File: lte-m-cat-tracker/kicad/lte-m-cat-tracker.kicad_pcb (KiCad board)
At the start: 2 copper layers, 30 x 35 mm, 32 parts, among them J1 JST-GH-1.25mm-2P, J2 USB-C-16P, SW1 MSK12C02, U1 SIM7080G-M, U2 ESP32-C3, U3 LIS2DW12TR, U4 TP4056, U5 XC6220B331MR-G

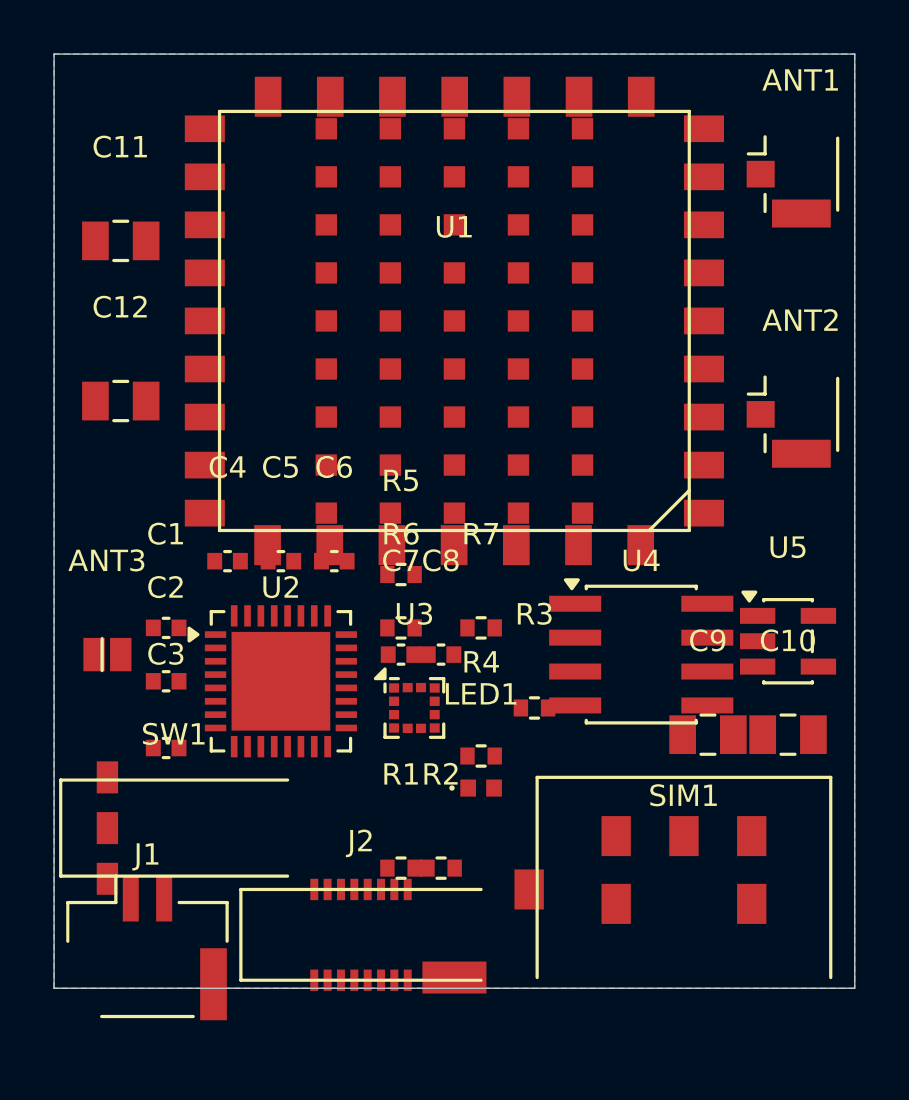
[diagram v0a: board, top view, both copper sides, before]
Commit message: lte-m-cat-tracker: PCB配置最適化・DRC短絡解消中
- PLACEMENTS全面再設計: SIM1右下端配置・SW1左側中段配置
- shorting_items: 6→1件に削減
- courtyards_overlap: 15→7件に削減
- 判明した実寸情報:
  - C9/C10 (C_0402): pad offset±0.95mm, courtyard 3.4×1.96mm
  - U4 SOIC-8: CrtYd 7.40×5.40mm (fp_lineで定義)
  - U5 SOT-23-5: CrtYd 4.10×3.40mm (fp_lineで定義)
  - generate_pcb.pyはfp_lineを未コピー → U4/U5のCrtYdがPCBに未反映

残課題:
- C9/C10短絡(1件): 0.95mm padのため3.1mm以上の間隔が必要
- U4 CrtYd 7.40×5.40mm → C9/C10の配置に影響
- generate_pcb.py の fp_line コピー対応が必要

Co-Authored-By: Claude Sonnet 4.6 <noreply@anthropic.com>
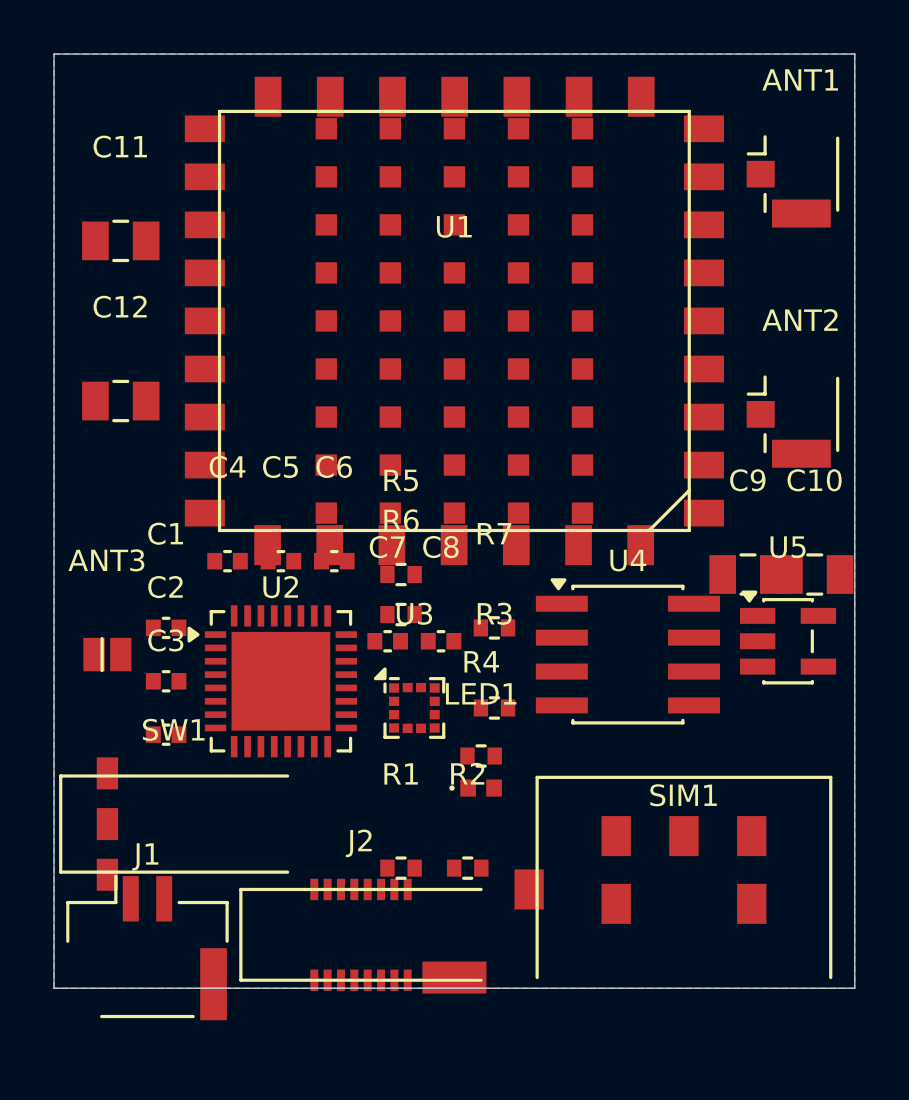
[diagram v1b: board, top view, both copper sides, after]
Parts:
- moved C9 6.18 mm to (26.0, 19.5)
- moved C10 6.08 mm to (28.5, 19.5)
- moved R3 1.50 mm to (16.5, 24.5)
- moved R2 1.00 mm to (15.5, 30.5)
- moved C7 0.71 mm to (12.5, 22.0)
- moved C3 0.50 mm to (4.20, 25.5)
- moved C8 0.50 mm to (14.5, 22.0)
- moved R6 0.50 mm to (13.0, 21.0)
- moved R7 0.50 mm to (16.5, 21.5)
- moved U4 0.50 mm to (21.5, 22.5)
- moved SW1 0.15 mm to (4.50, 28.9)
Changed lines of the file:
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@@
 	(footprint ""
 		(layer "F.Cu")
-		(at 4.2000 26.0000)
+		(at 4.2000 25.5000)
 		(property "Reference" "C3"
 			(at 0 -3.5 0)
@@
 	(footprint ""
 		(layer "F.Cu")
-		(at 13.0000 21.5000)
+		(at 13.0000 21.0000)
 		(property "Reference" "R6"
 			(at 0 -3.5 0)
@@
 	(footprint ""
 		(layer "F.Cu")
-		(at 16.0000 21.5000)
+		(at 16.5000 21.5000)
 		(property "Reference" "R7"
 			(at 0 -3.5 0)
@@
 	(footprint ""
 		(layer "F.Cu")
-		(at 13.0000 22.5000)
+		(at 12.5000 22.0000)
 		(property "Reference" "C7"
 			(at 0 -3.5 0)
@@
 	(footprint ""
 		(layer "F.Cu")
-		(at 14.5000 22.5000)
+		(at 14.5000 22.0000)
 		(property "Reference" "C8"
 			(at 0 -3.5 0)
@@
 	(footprint ""
 		(layer "F.Cu")
-		(at 22.0000 22.5000)
+		(at 21.5000 22.5000)
 		(property "Reference" "U4"
 			(at 0 -3.5 0)
@@
 	(footprint ""
 		(layer "F.Cu")
-		(at 24.5000 25.5000)
+		(at 26.0000 19.5000)
 		(property "Reference" "C9"
 			(at 0 -3.5 0)
@@
 	(footprint ""
 		(layer "F.Cu")
-		(at 27.5000 25.5000)
+		(at 28.5000 19.5000)
 		(property "Reference" "C10"
 			(at 0 -3.5 0)
@@
 	(footprint ""
 		(layer "F.Cu")
-		(at 18.0000 24.5000)
+		(at 16.5000 24.5000)
 		(property "Reference" "R3"
 			(at 0 -3.5 0)
@@
 	(footprint ""
 		(layer "F.Cu")
-		(at 4.5000 29.0000)
+		(at 4.5000 28.8500)
 		(property "Reference" "SW1"
 			(at 0 -3.5 0)
@@
 	(footprint ""
 		(layer "F.Cu")
-		(at 14.5000 30.5000)
+		(at 15.5000 30.5000)
 		(property "Reference" "R2"
 			(at 0 -3.5 0)

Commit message: lte-m-cat-tracker: DRC短絡0件・courtyard重なり0件に解消
- 短絡(C9pad2 GND ↔ C10pad1 +3.3V): C9を移動して解消
- courtyard重なり7件: C9/C10/C7/J1/J2を再配置して全解消
- DRC 149件 → 142件（shorting_items/courtyards_overlap = 0）
- 残り142件はシルク・クリアランス・エッジ系（配線前段階として正常）
- 次: 配線（ルーティング）フェーズ

Co-Authored-By: Claude Sonnet 4.6 <noreply@anthropic.com>
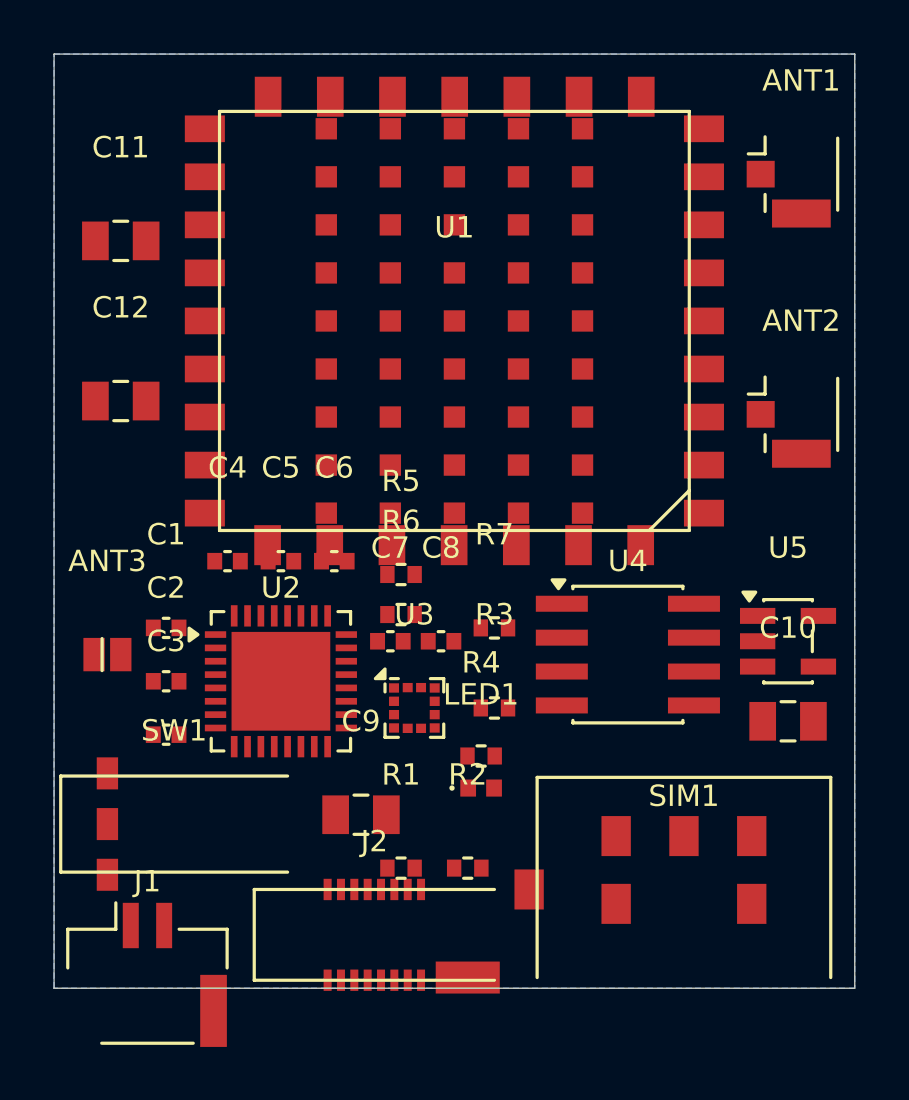
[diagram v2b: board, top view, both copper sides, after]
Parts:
- moved C9 17.1 mm to (11.5, 28.5)
- moved C10 5.59 mm to (27.5, 25.0)
- moved J1 1.00 mm to (3.50, 34.5)
- moved J2 0.50 mm to (12.0, 33.0)
- moved C7 0.10 mm to (12.6, 22.0)
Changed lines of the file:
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@@
 	(footprint ""
 		(layer "F.Cu")
-		(at 12.5000 22.0000)
+		(at 12.6000 22.0000)
 		(property "Reference" "C7"
 			(at 0 -3.5 0)
@@
 	(footprint ""
 		(layer "F.Cu")
-		(at 26.0000 19.5000)
+		(at 11.5000 28.5000)
 		(property "Reference" "C9"
 			(at 0 -3.5 0)
@@
 	(footprint ""
 		(layer "F.Cu")
-		(at 28.5000 19.5000)
+		(at 27.5000 25.0000)
 		(property "Reference" "C10"
 			(at 0 -3.5 0)
@@
 	(footprint ""
 		(layer "F.Cu")
-		(at 3.5000 33.5000)
+		(at 3.5000 34.5000)
 		(property "Reference" "J1"
 			(at 0 -3.5 0)
@@
 	(footprint ""
 		(layer "F.Cu")
-		(at 11.5000 33.0000)
+		(at 12.0000 33.0000)
 		(property "Reference" "J2"
 			(at 0 -3.5 0)

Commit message: lte-m-cat-tracker: 配置最終調整・GNDゾーン追加
- C5/C6をy=19.0→19.8、R5をy=19.5→19.8に移動
  (U1 SIM7080G-M底面パッドとの0mm重複を全解消)
- R1をy=30.5→30.2、R2をy=30.5→29.8に移動
  (J2 USB-Cとのクリアランス 0.08mm→0.38mm以上に改善)
- F.Cu GNDカッパーフィルゾーン追加 (B.Cuは既存)
  → GND未配線86→59本に削減(27本自動解決)
- 致命的違反(shorts/courtyard/0mm): 0件を維持
- DRC: 142件→131件、未配線: 86→59本
- 次フェーズ: KiCad GUIで配線(VBAT/3V3/RF/UART/I2C/SIM)

Co-Authored-By: Claude Sonnet 4.6 <noreply@anthropic.com>
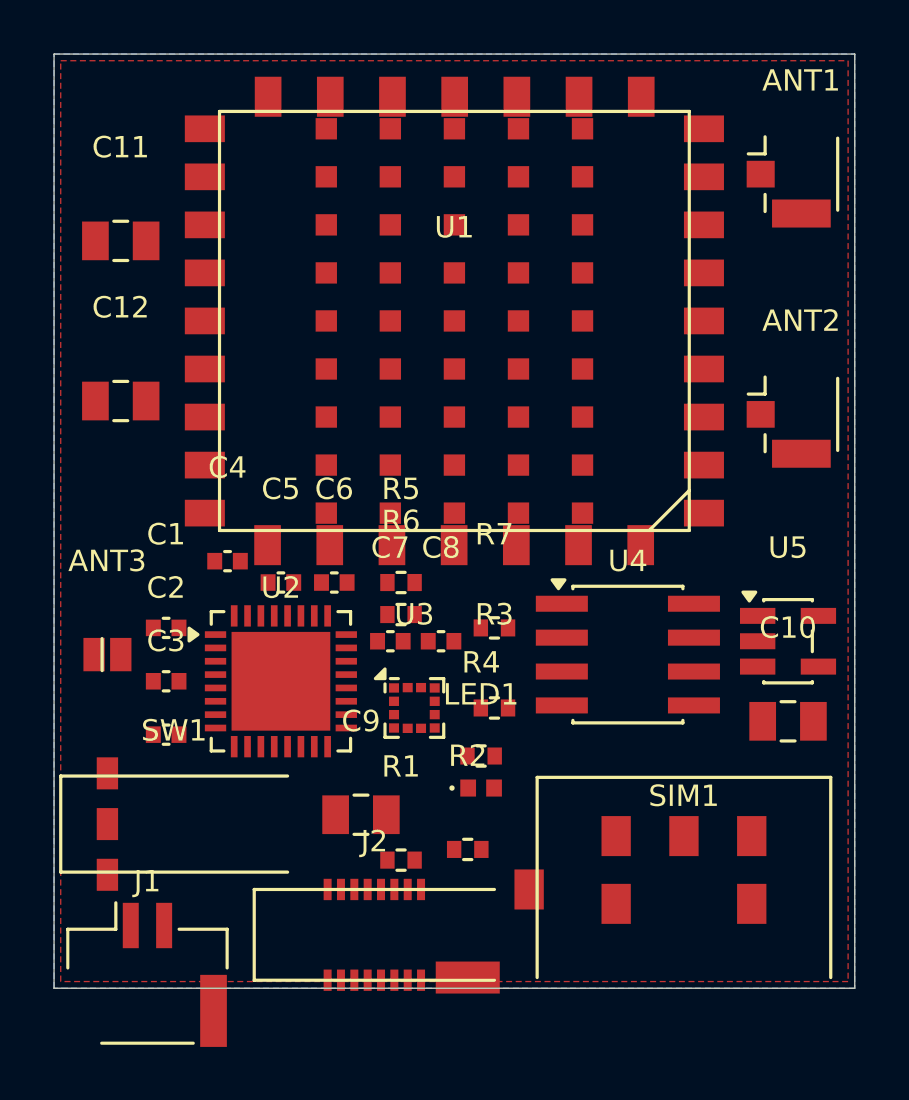
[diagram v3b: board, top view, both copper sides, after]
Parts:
- moved C5 0.80 mm to (8.50, 19.8)
- moved C6 0.80 mm to (10.5, 19.8)
- moved R2 0.70 mm to (15.5, 29.8)
- moved R1 0.30 mm to (13.0, 30.2)
- moved R5 0.30 mm to (13.0, 19.8)
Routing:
- added copper zone on F.Cu, net GND

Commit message: route_pcb_v5.py: 短絡8→0件達成（2026-06-06）
修正内容:
- SIM_TXD: B.Cu水平y=20.5→20.5（維持）、via x=9.25→11.0、B.Cu終端y=20.5
- SIM_TXD: SIM_TXD縦 x=11.0→11.5に移動（SIM_RXD via用スペース確保）
- +3.3V U2接続: via(7.5,19.6)→via(6.5,19.6)、x=7.0→6.5へ移動（C4.pad2回避）
- +3.3V U3接続: B.Cu縦スタブ x=11.5→11.8（U2右側パッドとの距離確保）
- SIM_STATUS: x=5.8→維持
- SIM_RXD: B.Cu縦x=8.75をy=20.0で止める（thermal pad干渉回避・GUI手動接続必要）

残り作業:
- SIM_RXD U2.pad28接続（KiCad GUI手動）
- VUSB接続（GUI手動）
- RF配線3本（GUI手動）

Co-Authored-By: Claude Sonnet 4.6 <noreply@anthropic.com>
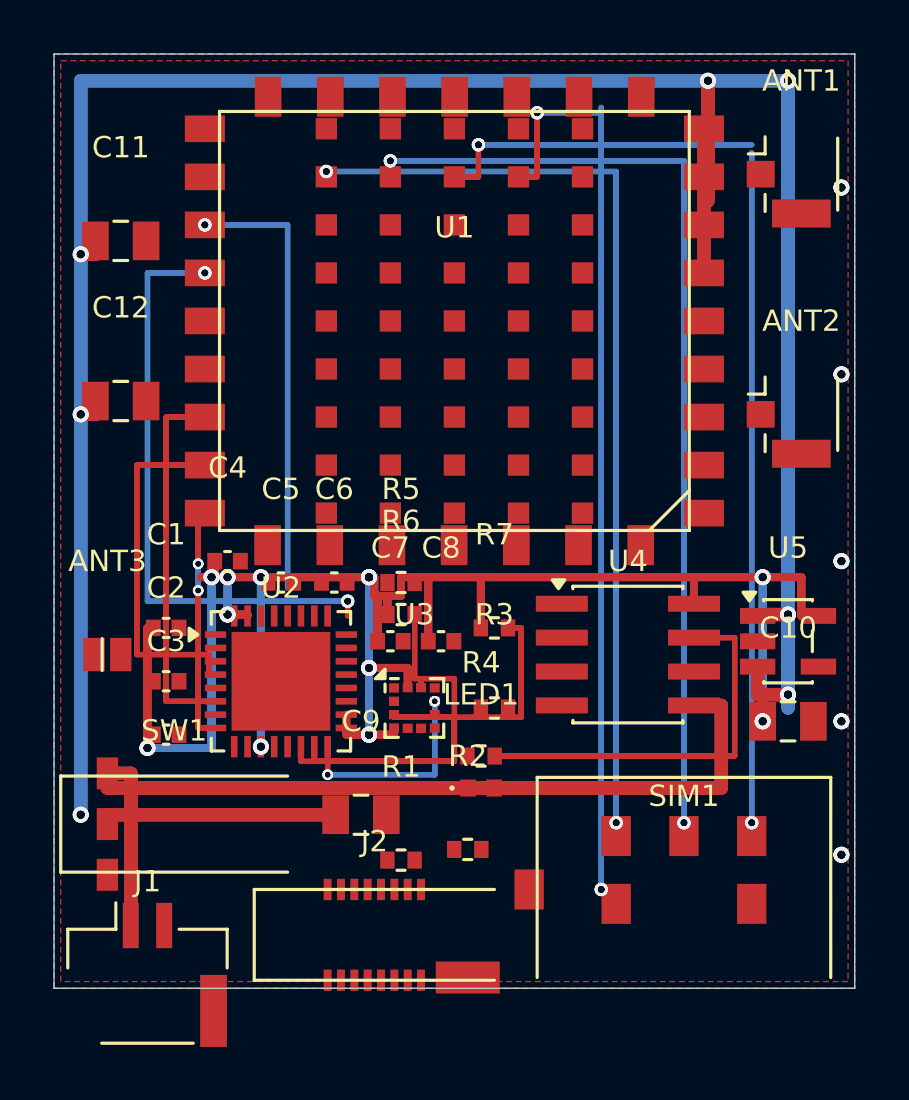
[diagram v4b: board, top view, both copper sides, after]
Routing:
- net VBAT_SW: track 0.00 -> 203.8 mm, vias 0 -> 14
- net +3.3V: track 0.00 -> 159.7 mm, vias 0 -> 26
- net SIM_CLK: track 0.00 -> 75.9 mm, vias 0 -> 4
- net SIM_DATA: track 0.00 -> 73.8 mm, vias 0 -> 4
- net SIM_VDD: track 0.00 -> 71.9 mm, vias 0 -> 4
- net SIM_RST: track 0.00 -> 71.8 mm, vias 0 -> 4
- net VBAT: track 0.00 -> 68.5 mm
- net SIM_TXD: track 0.00 -> 45.0 mm, vias 0 -> 4
- net I2C_SCL: track 0.00 -> 36.8 mm
- net SIM_RXD: track 0.00 -> 33.4 mm, vias 0 -> 2
- net CHRG: track 0.00 -> 29.9 mm
- net SIM_RESETN: track 0.00 -> 27.9 mm
- net I2C_SDA: track 0.00 -> 27.3 mm
- net SIM_STATUS: track 0.00 -> 26.7 mm
- net SIM_PWRKEY: track 0.00 -> 17.9 mm, vias 0 -> 4
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
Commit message: route_pcb_v7.py: 短絡0件達成（2026-06-06）
- SIM_RXD via位置修正: (8.75,20.3)→(8.75,21.05) でC5.pad2 GND短絡解消
- WIFI_ANT: スクリプトルーティング不可（+3.3V B.Cu x=5.9 と thermal pad の隙間が不足）
  → KiCad GUI手動配線に移行
- DRC結果: shorting_items=0件 / 未配線13件（WIFI_ANT含む）
- DESIGN.md: 進捗・次セッション手順を更新

Co-Authored-By: Claude Sonnet 4.6 <noreply@anthropic.com>
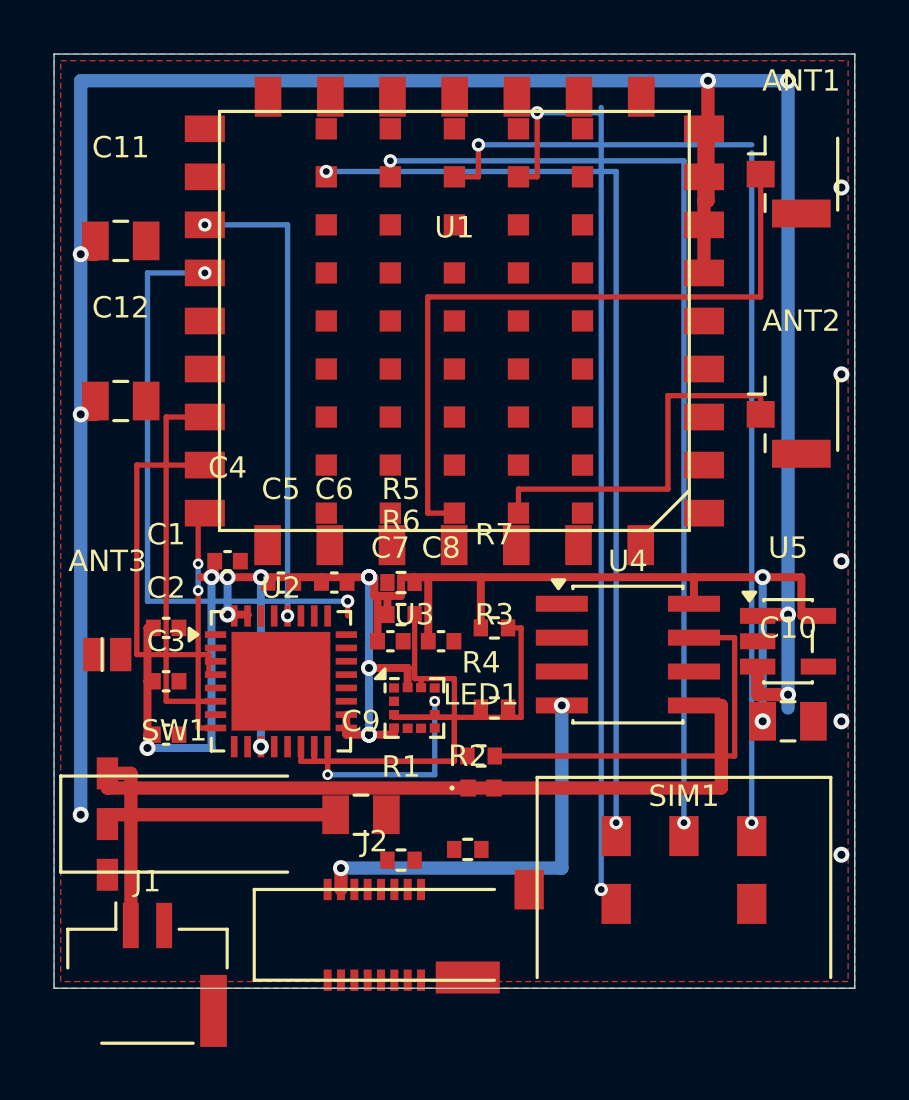
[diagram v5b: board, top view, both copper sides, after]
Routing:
- net VBAT_SW: track 203.8 -> 101.9 mm, vias 14 -> 7
- net +3.3V: track 159.7 -> 79.9 mm, vias 26 -> 13
- net SIM_CLK: track 75.9 -> 37.9 mm, vias 4 -> 2
- net SIM_DATA: track 73.8 -> 36.9 mm, vias 4 -> 2
- net SIM_VDD: track 71.9 -> 36.0 mm, vias 4 -> 2
- net SIM_RST: track 71.8 -> 35.9 mm, vias 4 -> 2
- net VBAT: track 68.5 -> 34.2 mm
- net LTE_ANT: track 0.00 -> 26.2 mm
- net SIM_TXD: track 45.0 -> 22.5 mm, vias 4 -> 2
- net I2C_SCL: track 36.8 -> 18.4 mm
- net SIM_RXD: track 33.4 -> 17.8 mm
- net VUSB: track 0.00 -> 15.2 mm, vias 0 -> 2
- net CHRG: track 29.9 -> 14.9 mm
- net GNSS_ANT: track 0.00 -> 14.2 mm
- net SIM_RESETN: track 27.9 -> 14.0 mm
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
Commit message: route_pcb_v8.py: WIFI_ANT配線追加・SIM短絡問題の根本原因特定（2026-06-06）
- route_pcb_v8.py 新規作成: WIFI_ANT スクリプト配線を初めて実装
  via(6.05,21.75)→B.Cu→via(1.75,23.8)→F.Cu→ANT3.pad1(1.5,22.5)
- +3.3V C1/C2/C3供給: via(5.9,19.6)削除→x=7.75 B.Cu延長経由に変更
- 未配線0件達成（WIFI_ANT含む全配線完了）

残課題: SIM信号 ↔ U2左側パッド(0.8×0.25mm,x=5.65-6.45)の物理ショート
v7では via(5.9,19.6)存在でDRCが solder_mask_bridge として分類していたが
v8でvia削除後に shorting_items として正しく検出。次セッションで修正予定。

Co-Authored-By: Claude Sonnet 4.6 <noreply@anthropic.com>
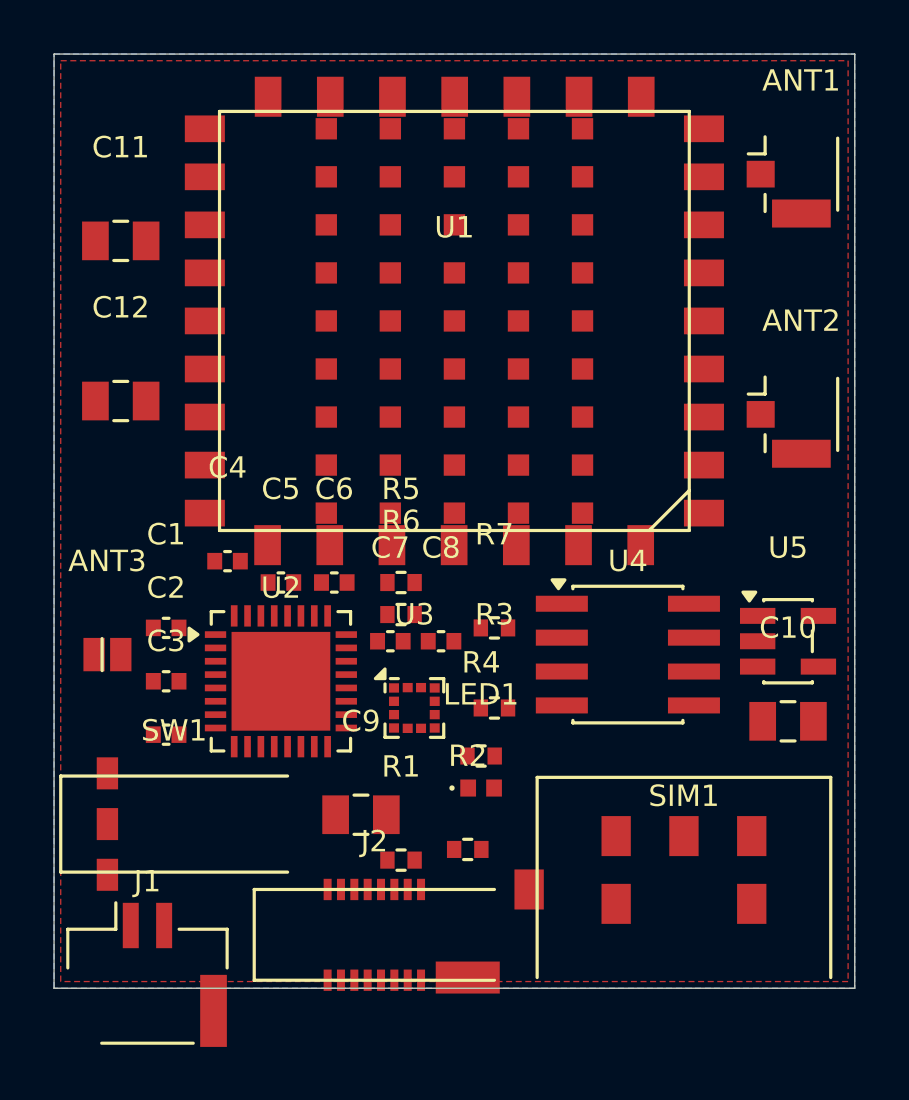
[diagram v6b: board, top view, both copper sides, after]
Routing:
- net VBAT_SW: track 101.9 -> 0.00 mm, vias 7 -> 0
- net +3.3V: track 79.9 -> 0.00 mm, vias 13 -> 0
- net SIM_CLK: track 37.9 -> 0.00 mm, vias 2 -> 0
- net SIM_DATA: track 36.9 -> 0.00 mm, vias 2 -> 0
- net SIM_VDD: track 36.0 -> 0.00 mm, vias 2 -> 0
- net SIM_RST: track 35.9 -> 0.00 mm, vias 2 -> 0
- net VBAT: track 34.2 -> 0.00 mm
- net LTE_ANT: track 26.2 -> 0.00 mm
- net SIM_TXD: track 22.5 -> 0.00 mm, vias 2 -> 0
- net I2C_SCL: track 18.4 -> 0.00 mm
- net SIM_RXD: track 17.8 -> 0.00 mm, vias 2 -> 0
- net VUSB: track 15.2 -> 0.00 mm, vias 2 -> 0
- net CHRG: track 14.9 -> 0.00 mm
- net GNSS_ANT: track 14.2 -> 0.00 mm
- net SIM_RESETN: track 14.0 -> 0.00 mm
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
